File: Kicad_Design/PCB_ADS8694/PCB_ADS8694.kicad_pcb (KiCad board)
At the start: 2 copper layers, 46 parts, among them J1 Screw_Terminal_01x03_Alimenta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, J4 Conn_02x06_Male_Pmod_Spartan6, J5 Screw_Terminal_01x02_CH3, J6 Screw_Terminal_01x02_CH2, J7 Screw_Terminal_01x02_CH1, J8 Screw_Terminal_01x02_CH0, U1 LM7805_TO220, U2 AD8221, U3 AD8221, U4 ADS8694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

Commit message: PCB V1
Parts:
- moved J1 1.15 mm to (147.4, 122.3)
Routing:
- net VCC: track 226.6 -> 227.7 mm
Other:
- board text added: "UNSL"

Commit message: Se cambia orientacion de bornera +-12V, con esto se evita usar vias para unir plano agnd. Se agregan vias para unir agnd con dgnd
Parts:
- moved C1 12.9 mm to (168.5, 123.8)
- moved J1 12.4 mm to (159.8, 122.3), turned to 180 degrees
- moved U1 9.67 mm to (177.5, 124.5)
- moved C3 1.94 mm to (188.2, 126.3)
- moved J4 1.38 mm to (195.9, 112.5)
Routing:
- net REFSEL: track 25.6 -> 13.5 mm, vias 2 -> 1
- net AVDD: track 64.3 -> 56.6 mm
- net VSS: track 189.5 -> 196.9 mm
- net VCC: track 227.7 -> 231.6 mm
- net GNDD: track 30.8 -> 34.1 mm, vias 0 -> 1
- net SDI: track 62.1 -> 64.7 mm
- net SDO: track 33.1 -> 34.5 mm
- net SCLK: track 36.5 -> 37.9 mm
- net CS: track 40.0 -> 41.4 mm
- net ALARM: track 29.6 -> 31.0 mm
- net RST-PD: track 53.4 -> 54.0 mm
- added copper zone on F.Cu, net GNDD
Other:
- board text added: "Luciano Villarreal - UNSL"
- board text removed: "Luciano Villarreal"
- board text removed: "UNSL"

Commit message: Se agranda el ancho de pista canal 0, para efectauar mediciones con mayor facilidad
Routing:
- net AIN_0P: track 14.6 -> 20.5 mm
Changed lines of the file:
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@@
     (thickness 1.6)
     (drawings 38)
-    (tracks 366)
+    (tracks 372)
     (zones 0)
     (modules 46)
@@
     (user_trace_width 0.3)
     (trace_clearance 0.2)
-    (zone_clearance 0.1)
+    (zone_clearance 0.5)
     (zone_45_only no)
     (trace_min 0.2)
@@
   (segment (start 180.667499 95.242501) (end 181.872501 95.242501) (width 0.4) (layer F.Cu) (net 37))
   (segment (start 180.66 95.25) (end 180.667499 95.242501) (width 0.3) (layer F.Cu) (net 37))
-  (segment (start 181.03 98.13) (end 177.01 98.13) (width 0.4) (layer F.Cu) (net 37))
-  (segment (start 182.61 96.55) (end 181.03 98.13) (width 0.4) (layer F.Cu) (net 37))
   (segment (start 177.01 98.13) (end 176.455 97.575) (width 0.4) (layer F.Cu) (net 37))
   (segment (start 181.872501 95.242501) (end 182.61 95.98) (width 0.4) (layer F.Cu) (net 37))
+  (segment (start 177.01 98.13) (end 177.03 98.13) (width 0.25) (layer F.Cu) (net 37))
+  (segment (start 181.03 98.13) (end 177.01 98.13) (width 0.4) (layer F.Cu) (net 37))
+  (segment (start 176.455 97.575) (end 176.455 97.585) (width 0.25) (layer F.Cu) (net 37))
+  (segment (start 176.455 97.585) (end 177.37 98.5) (width 0.4) (layer F.Cu) (net 37))
+  (segment (start 180.66 98.5) (end 181.575 97.585) (width 0.4) (layer F.Cu) (net 37))
+  (segment (start 177.37 98.5) (end 180.66 98.5) (width 0.4) (layer F.Cu) (net 37))
+  (segment (start 182.61 96.55) (end 181.575 97.585) (width 0.4) (layer F.Cu) (net 37))
+  (segment (start 181.575 97.585) (end 181.03 98.13) (width 0.4) (layer F.Cu) (net 37))
   (zone (net 2) (net_name REFSEL) (layer F.Cu) (hatch edge 0.508)
     (connect_pads (clearance 0.1))
@@
     (polygon
       (pts
-        (xy 178.39 87.51) (xy 179.01 87.51) (xy 179.01 89) (xy 182.75 89) (xy 182.75 90.5)
-        (xy 191.78 90.5) (xy 191.78 100.22) (xy 177.97 100.22) (xy 177.97 87.51)
+        (xy 178.43 96.84) (xy 178.26 87.3) (xy 179.01 87.35) (xy 179.01 89) (xy 182.75 89)
+        (xy 182.75 90.5) (xy 191.78 90.5) (xy 191.78 100.22) (xy 172.39 100.18) (xy 172.36 96.81)
       )
     )
@@
     )
   )
-  (zone (net 2) (net_name REFSEL) (layer F.Cu) (hatch edge 0.508)
+  (zone (net 5) (net_name GNDD) (layer F.Cu) (hatch edge 0.508)
     (connect_pads (clearance 0.1))
-    (min_thickness 0.1)
+    (min_thickness 0.254)
     (fill yes (arc_segments 32) (thermal_gap 0.508) (thermal_bridge_width 0.508))
     (polygon
       (pts
-        (xy 119.5 81.13) (xy 119.5 90.65) (xy 119.5 119.6) (xy 119.5 131.08) (xy 192.53 131.08)
-        (xy 192.53 99.17) (xy 178.51 99.17) (xy 178.51 81.12) (xy 143.99 81.12)
+        (xy 196.925 102.675) (xy 192.75 98.45) (xy 192.75 106.2) (xy 197.3 106.2) (xy 197.3 103.05)
       )
     )
   )
-  (zone (net 5) (net_name GNDD) (layer F.Cu) (hatch edge 0.508)
+  (zone (net 2) (net_name REFSEL) (layer F.Cu) (hatch edge 0.508)
     (connect_pads (clearance 0.1))
-    (min_thickness 0.254)
+    (min_thickness 0.1)
     (fill yes (arc_segments 32) (thermal_gap 0.508) (thermal_bridge_width 0.508))
     (polygon
       (pts
-        (xy 196.925 102.675) (xy 192.75 98.45) (xy 192.75 106.2) (xy 197.3 106.2) (xy 197.3 103.05)
+        (xy 119.5 81.13) (xy 119.5 90.65) (xy 119.5 119.6) (xy 119.5 131.08) (xy 192.53 131.08)
+        (xy 192.53 99.17) (xy 178.51 99.17) (xy 178.51 81.12) (xy 143.99 81.12)
       )
     )

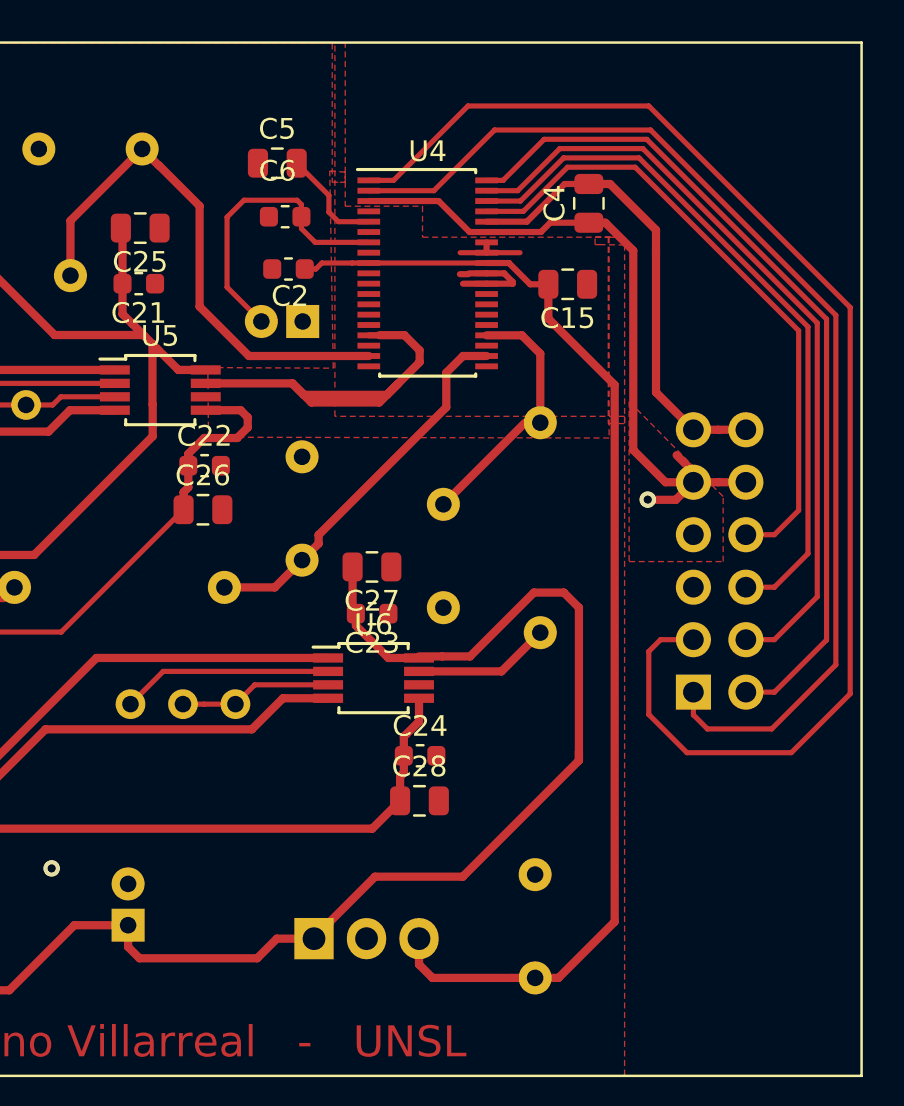
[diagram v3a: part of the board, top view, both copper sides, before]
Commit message: Cambios en conector pmod
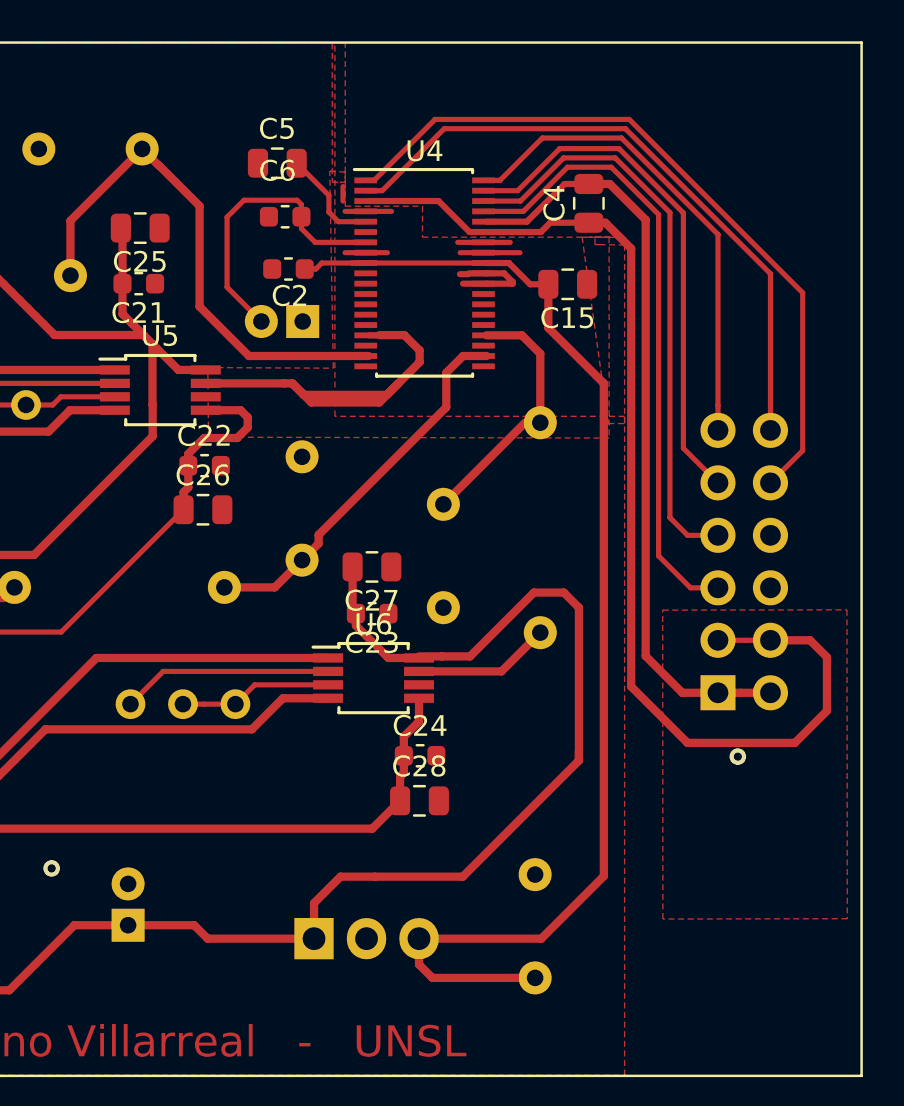
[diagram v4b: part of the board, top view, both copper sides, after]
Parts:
- U4: value ADS8694 -> ADS8694_Vers2
- moved J4 1.19 mm to (197.1, 112.5)
- moved U4 0.15 mm to (182.8, 92.2)
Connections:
- J4 pad 1: RST-PD -> VDD
- J4 pad 10: GNDD -> SDI
- J4 pad 11: VDD -> CS
- J4 pad 12: VDD -> RST-PD
- J4 pad 2: CS -> VDD
- J4 pad 3: SDI -> GNDD
- J4 pad 4: SCLK -> GNDD
- J4 pad 5: (no net) -> ALARM
- J4 pad 6: SDO -> (no net)
- J4 pad 7: (no net) -> SDO
- J4 pad 8: ALARM -> (no net)
- J4 pad 9: GNDD -> SCLK
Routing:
- net SDI: track 64.7 -> 35.7 mm
- net RST-PD: track 54.0 -> 31.3 mm
- net GNDD: track 34.1 -> 54.7 mm
- net CS: track 41.4 -> 23.6 mm
- net VDD: track 22.8 -> 37.1 mm
- net SCLK: track 37.9 -> 25.6 mm
- net REFSEL: track 13.5 -> 20.6 mm
- net SDO: track 34.5 -> 28.4 mm
- net AVDD: track 56.6 -> 59.4 mm
- net ALARM: track 31.0 -> 30.3 mm
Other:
- board text added: "ALARM NC"
- board text added: "CS RST-PD"
- board text added: "SCLK SDI"
- board text added: "SDO NC"
- board text removed: "NC ALARM"
- board text removed: "NC SDO"
- board text removed: "RST-PD CS"
- board text removed: "SDI SCLK"

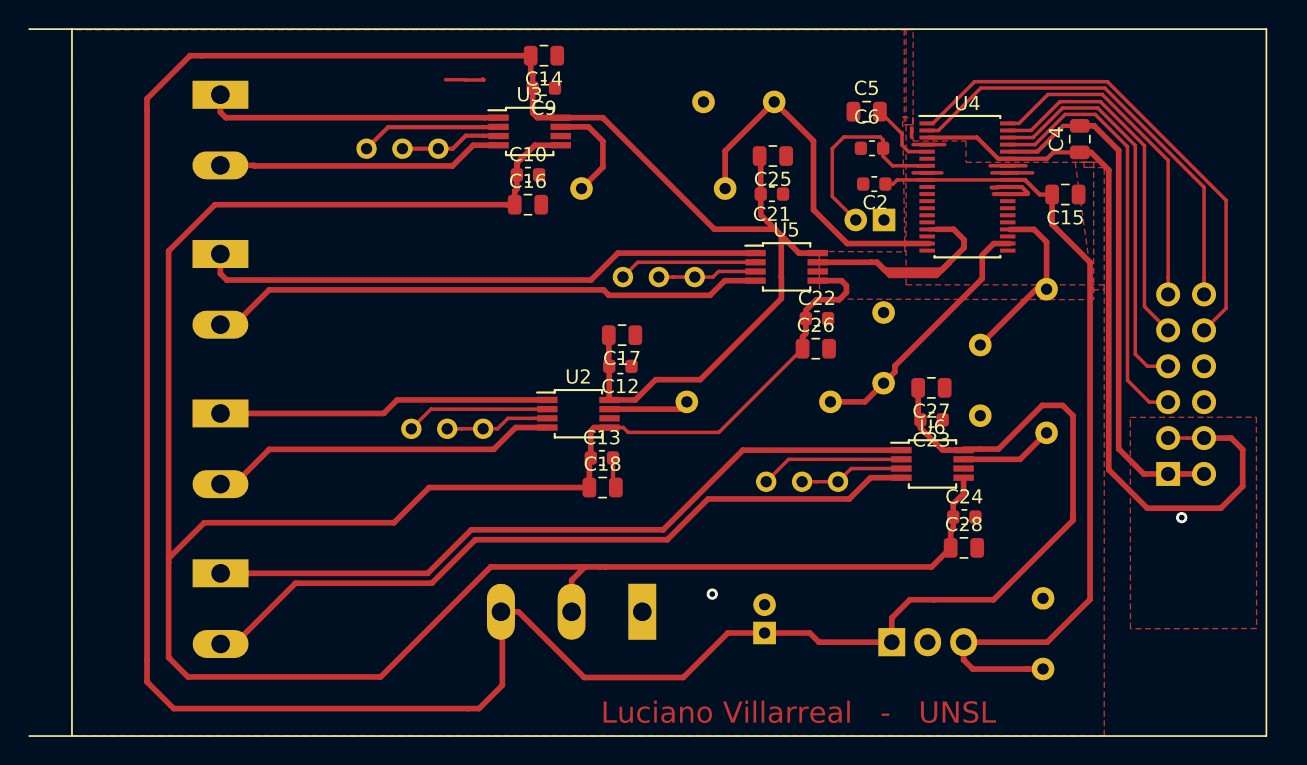
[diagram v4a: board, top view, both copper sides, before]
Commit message: Capacitores 10uF de smd a THT
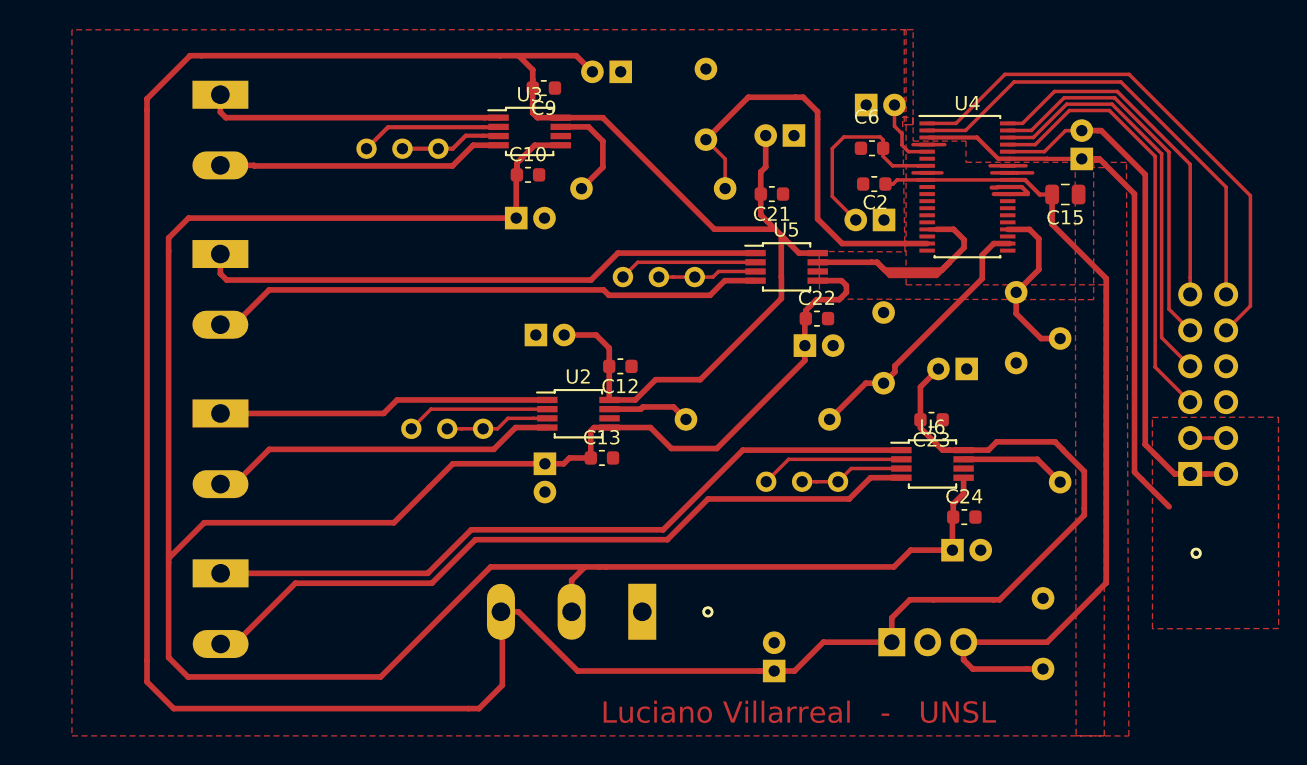
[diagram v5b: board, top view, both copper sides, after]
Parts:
- C14, C16, C17, C18, C25, C26, C27, C28, C4, C5: footprint Capacitor_SMD:C_0805_2012Metric -> Capacitor_THT:CP_Radial_D5.0mm_P2.00mm; moved to B.Cu
- moved C17 6.10 mm to (152.3, 102.7), turned to 0 degrees
- moved C14 5.55 mm to (158.3, 84.1)
- moved C8 5.52 mm to (164.3, 88.9), turned to 90 degrees
- moved C29 4.51 mm to (186.3, 99.7)
- moved C18 4.41 mm to (153.0, 111.8), turned to 270 degrees
- moved R3 3.62 mm to (189.4, 103.0)
- moved C27 2.83 mm to (182.8, 105.1)
- moved C1 2.77 mm to (169.2, 126.5)
- moved C25 2.08 mm to (170.6, 88.6)
- moved J4 1.56 mm to (198.6, 112.5)
- moved C4 1.40 mm to (190.9, 90.3)
- moved C16 1.26 mm to (150.9, 94.5)
- moved R2 1.24 mm to (173.1, 108.7)
- moved C28 0.83 mm to (181.8, 117.9)
- moved C26 0.80 mm to (171.3, 103.5)
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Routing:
- net GNDD: track 54.7 -> 41.9 mm
- net VCC: track 231.2 -> 238.4 mm
- net REFSEL: track 20.6 -> 14.9 mm
- net AIN_1P: track 25.5 -> 29.6 mm
- net SDI: track 35.7 -> 38.1 mm
- net RST-PD: track 31.3 -> 33.2 mm
- net VSS: track 196.9 -> 198.7 mm
- net SCLK: track 25.6 -> 27.2 mm
- net CS: track 23.6 -> 25.2 mm
- net AVDD: track 59.4 -> 60.4 mm
- net Net-(R3-Pad2): track 6.65 -> 7.50 mm
- net ALARM: track 30.3 -> 31.2 mm
- net SDO: track 28.4 -> 29.2 mm
- net AIN_2P: track 18.6 -> 19.1 mm
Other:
- board text removed: "4 CANALES DIFERENCIALES ADS8694 COMUNICACIÓN SPI"

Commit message: Cambios varios, Version 1 funcional
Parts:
- removed J4: Conn_02x06_Male_Pmod_Spartan6, Connector_PinHeader_2.54mm:PinHeader_2x06_P2.54mm_Horizontal
- added J2: Conn_01x06_Male, Connector_PinHeader_2.54mm:PinHeader_1x06_P2.54mm_Vertical, B.Cu at (198.6, 112.4)
- added J3: Conn_01x06_Male, Connector_PinHeader_2.54mm:PinHeader_1x06_P2.54mm_Vertical, B.Cu at (202.8, 112.4)
- C15: footprint Capacitor_SMD:C_0805_2012Metric -> Capacitor_SMD:C_0603_1608Metric
- C3: value 0.1uF -> 100nF
- moved C1 1.92 mm to (169.2, 124.6)
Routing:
- net SDI: track 38.1 -> 48.6 mm
- net ALARM: track 31.2 -> 36.0 mm
- net AVDD: track 60.4 -> 55.7 mm
- net GNDD: track 41.9 -> 39.3 mm
- net RST-PD: track 33.2 -> 35.0 mm
- net VDD: track 37.3 -> 38.5 mm
- net VCC: track 238.4 -> 237.6 mm
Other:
- board text added: "AGND"
- board text added: "DGND DGND"
- board text added: "SCLK ALARM"
- board text added: "SDI NC"
- board text removed: "ALARM NC"
- board text removed: "GND"
- board text removed: "GND GND"
- board text removed: "SCLK SDI"

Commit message: version finalizada
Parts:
- moved C1 106.1 mm to (77.9, 70.5)
- moved C12 106.1 mm to (67.0, 50.9)
- moved C13 106.1 mm to (65.7, 57.4)
- moved C15 106.1 mm to (98.5, 38.8)
- moved C16 106.1 mm to (59.6, 40.4)
- moved C18 106.1 mm to (61.6, 57.8)
- moved C21 106.1 mm to (77.7, 38.7)
- moved C25 106.1 mm to (79.3, 34.6)
- moved C27 106.1 mm to (91.5, 51.1)
- moved C29 106.1 mm to (95.0, 45.7)
- moved J2 106.1 mm to (107.3, 58.4)
- moved J5 106.1 mm to (38.7, 65.5)
- moved R1 106.1 mm to (74.4, 38.3)
- moved RV3 106.1 mm to (77.3, 59.1)
- moved U2 106.1 mm to (64.0, 54.3)
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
